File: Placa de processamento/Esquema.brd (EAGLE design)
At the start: 145.1 x 89.8 mm, 12 parts

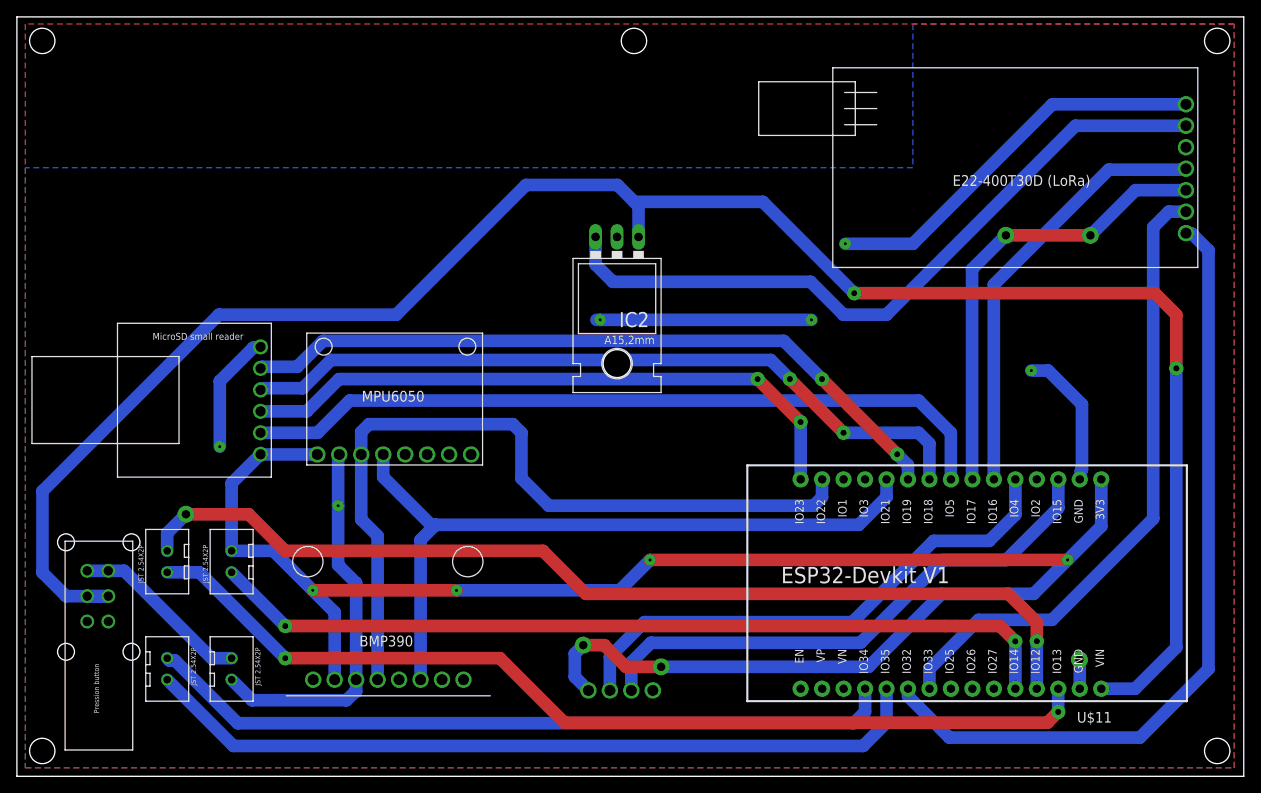
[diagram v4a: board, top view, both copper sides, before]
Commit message: Adicionado LED indicativo.
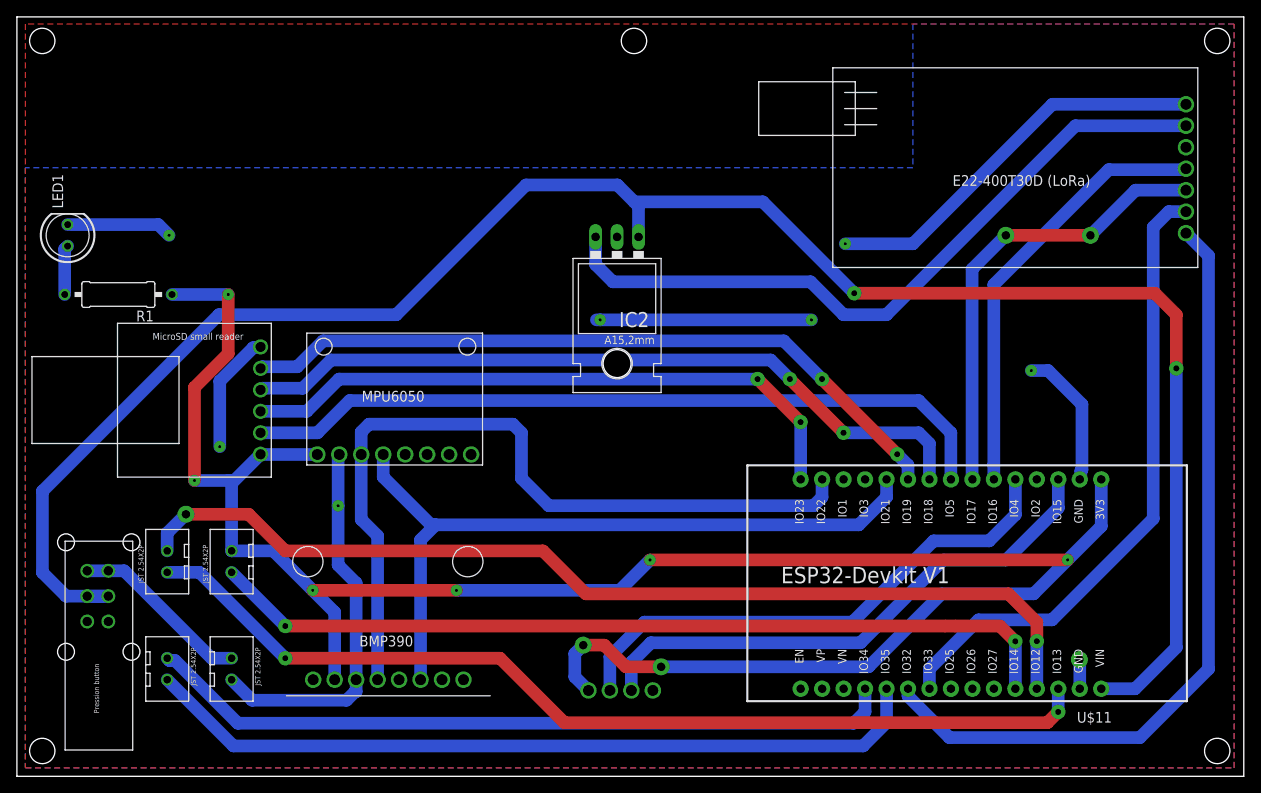
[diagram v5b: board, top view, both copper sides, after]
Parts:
- added LED1: (no value), led:LED5MM
- added R1: (no value), rcl:0309/12
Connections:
- new net N$4: LED1.A, R1.2
- net GND: now also LED1.K
- net N$3: now also R1.1
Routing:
- net N$3: track 214.8 -> 249.6 mm, vias 6 -> 8
- net GND: track 152.1 -> 164.6 mm, vias 7 -> 8
- net N$4: track 0.00 -> 5.87 mm
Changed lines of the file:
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@@
 <attribute name="VALUE" x="74.937" y="57.46" size="1.778" layer="27" ratio="10" rot="R180"/>
+</element>
+<element name="LED1" library="led" library_urn="urn:adsk.eagle:library:259" package="LED5MM" package3d_urn="urn:adsk.eagle:package:15799/2" value="" x="6" y="64" smashed="yes" rot="R90">
+<attribute name="NAME" x="5.4666" y="67.175" size="1.27" layer="25" ratio="10" rot="R90"/>
+<attribute name="POPULARITY" value="93" x="6" y="64" size="1.778" layer="27" rot="R90" display="off"/>
+<attribute name="VALUE" x="7.8034" y="67.2004" size="1.27" layer="27" ratio="10" rot="R90"/>
+</element>
+<element name="R1" library="rcl" library_urn="urn:adsk.eagle:library:334" package="0309/12" package3d_urn="urn:adsk.eagle:package:23571/1" value="" x="12" y="57" smashed="yes" rot="R180">
+<attribute name="NAME" x="16.191" y="55.095" size="1.27" layer="25" ratio="10" rot="R180"/>
+<attribute name="POPULARITY" value="8" x="12" y="57" size="1.778" layer="27" rot="R180" display="off"/>
+<attribute name="SPICEPREFIX" value="R" x="12" y="57" size="1.778" layer="27" rot="R180" display="off"/>
+<attribute name="VALUE" x="15.175" y="57.6858" size="1.27" layer="27" ratio="10" rot="R180"/>
 </element>
 </elements>
@@
 <wire x1="66" y1="11.77" x2="67.61" y2="10.16" width="1.5" layer="16"/>
 <wire x1="66" y1="14.518" x2="66" y2="11.77" width="1.5" layer="16"/>
+<contactref element="R1" pad="1"/>
+<wire x1="18.35" y1="57" x2="25" y2="57" width="1.5" layer="16"/>
+<via x="25" y="57" extent="1-16" drill="0.35"/>
+<wire x1="25.4" y1="34.671" x2="25.071" y2="35" width="1.5" layer="16"/>
+<wire x1="25.071" y1="35" x2="21" y2="35" width="1.5" layer="16"/>
+<via x="21" y="35" extent="1-16" drill="0.35"/>
+<wire x1="21" y1="35" x2="21" y2="46" width="1.5" layer="1"/>
+<wire x1="21" y1="46" x2="25" y2="50" width="1.5" layer="1"/>
+<wire x1="25" y1="50" x2="25" y2="57" width="1.5" layer="1"/>
 </signal>
 <signal name="N$5">
@@
 <contactref element="U$2" pad="M0"/>
 <contactref element="U$11" pad="21"/>
-<wire x1="132.850634375" y1="4.580634375" x2="140.97" y2="12.7" width="1.5" layer="16"/>
-<wire x1="140.97" y1="12.7" x2="140.97" y2="62.23" width="1.5" layer="16"/>
+<wire x1="140.97" y1="12.7" x2="132.850634375" y2="4.580634375" width="1.5" layer="16"/>
 <wire x1="105.42" y1="10.36" x2="105.42" y2="9.4843875" width="1.5" layer="16"/>
 <wire x1="105.42" y1="9.4843875" x2="110.323753125" y2="4.580634375" width="1.5" layer="16"/>
 <wire x1="110.323753125" y1="4.580634375" x2="132.850634375" y2="4.580634375" width="1.5" layer="16"/>
-<wire x1="140.97" y1="62.23" x2="138.975" y2="64.225" width="1.5" layer="16"/>
-<wire x1="138.975" y1="64.225" x2="138.318325" y2="64.225" width="1.5" layer="16"/>
-<wire x1="138.318325" y1="64.225" x2="138.303" y2="64.262" width="0" layer="19" extent="16-16"/>
+<wire x1="138.303" y1="64.262" x2="140.97" y2="61.595" width="1.5" layer="16"/>
+<wire x1="140.97" y1="61.595" x2="140.97" y2="12.7" width="1.5" layer="16"/>
 </signal>
 <signal name="N$13">
@@
 <wire x1="39.37" y1="44.45" x2="106.68" y2="44.45" width="1.5" layer="16"/>
 <wire x1="106.68" y1="44.45" x2="110.49" y2="40.64" width="1.5" layer="16"/>
-<wire x1="110.49" y1="40.64" x2="110.49" y2="35.56" width="1.5" layer="16"/>
-<wire x1="110.49" y1="35.56" x2="110.5" y2="35.13" width="0" layer="19" extent="16-16"/>
+<wire x1="110.49" y1="35.14" x2="110.5" y2="35.13" width="1.5" layer="16"/>
+<wire x1="110.49" y1="40.64" x2="110.49" y2="35.14" width="1.5" layer="16"/>
 </signal>
 <signal name="N$14">
@@
 <wire x1="97.79" y1="40.64" x2="106.68" y2="40.64" width="1.5" layer="16"/>
 <wire x1="106.68" y1="40.64" x2="107.95" y2="39.37" width="1.5" layer="16"/>
-<wire x1="107.95" y1="39.37" x2="107.95" y2="35.56" width="1.5" layer="16"/>
-<wire x1="107.95" y1="35.56" x2="107.96" y2="35.13" width="0" layer="19" extent="16-16"/>
+<wire x1="107.95" y1="35.14" x2="107.96" y2="35.13" width="1.5" layer="16"/>
+<wire x1="107.95" y1="39.37" x2="107.95" y2="35.14" width="1.5" layer="16"/>
 </signal>
 <signal name="N$16">
@@
 <vertex x="144" y="89"/>
 </polygon>
+<contactref element="LED1" pad="K"/>
+<wire x1="6" y1="65.27" x2="16.73" y2="65.27" width="1.5" layer="16"/>
+<wire x1="16.73" y1="65.27" x2="18" y2="64" width="1.5" layer="16"/>
+<via x="18" y="64" extent="1-16" drill="0.35"/>
+</signal>
+<signal name="N$4">
+<contactref element="R1" pad="2"/>
+<contactref element="LED1" pad="A"/>
+<wire x1="5.65" y1="57" x2="5.65" y2="62.38" width="1.5" layer="16"/>
+<wire x1="5.65" y1="62.38" x2="6" y2="62.73" width="1.5" layer="16"/>
 </signal>
 </signals>
